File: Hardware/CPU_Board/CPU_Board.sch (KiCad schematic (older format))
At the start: 45 parts, among them P1 CONN_01X02, P2 USB_B, P3 CONN_01X06, P4 CONN_01X01, P5 CONN_01X01, P6 CONN_01X01, P7 CONN_01X01, P8 CONN_01X01, P9 CONN_01X01, U1 UA78M05IDCY, U2 UA78M33CDCY, U3 STM32F411RETx, U4 FT232RL, U5 TRACO_POWER_TEL_2-0511, Y1 8MHz

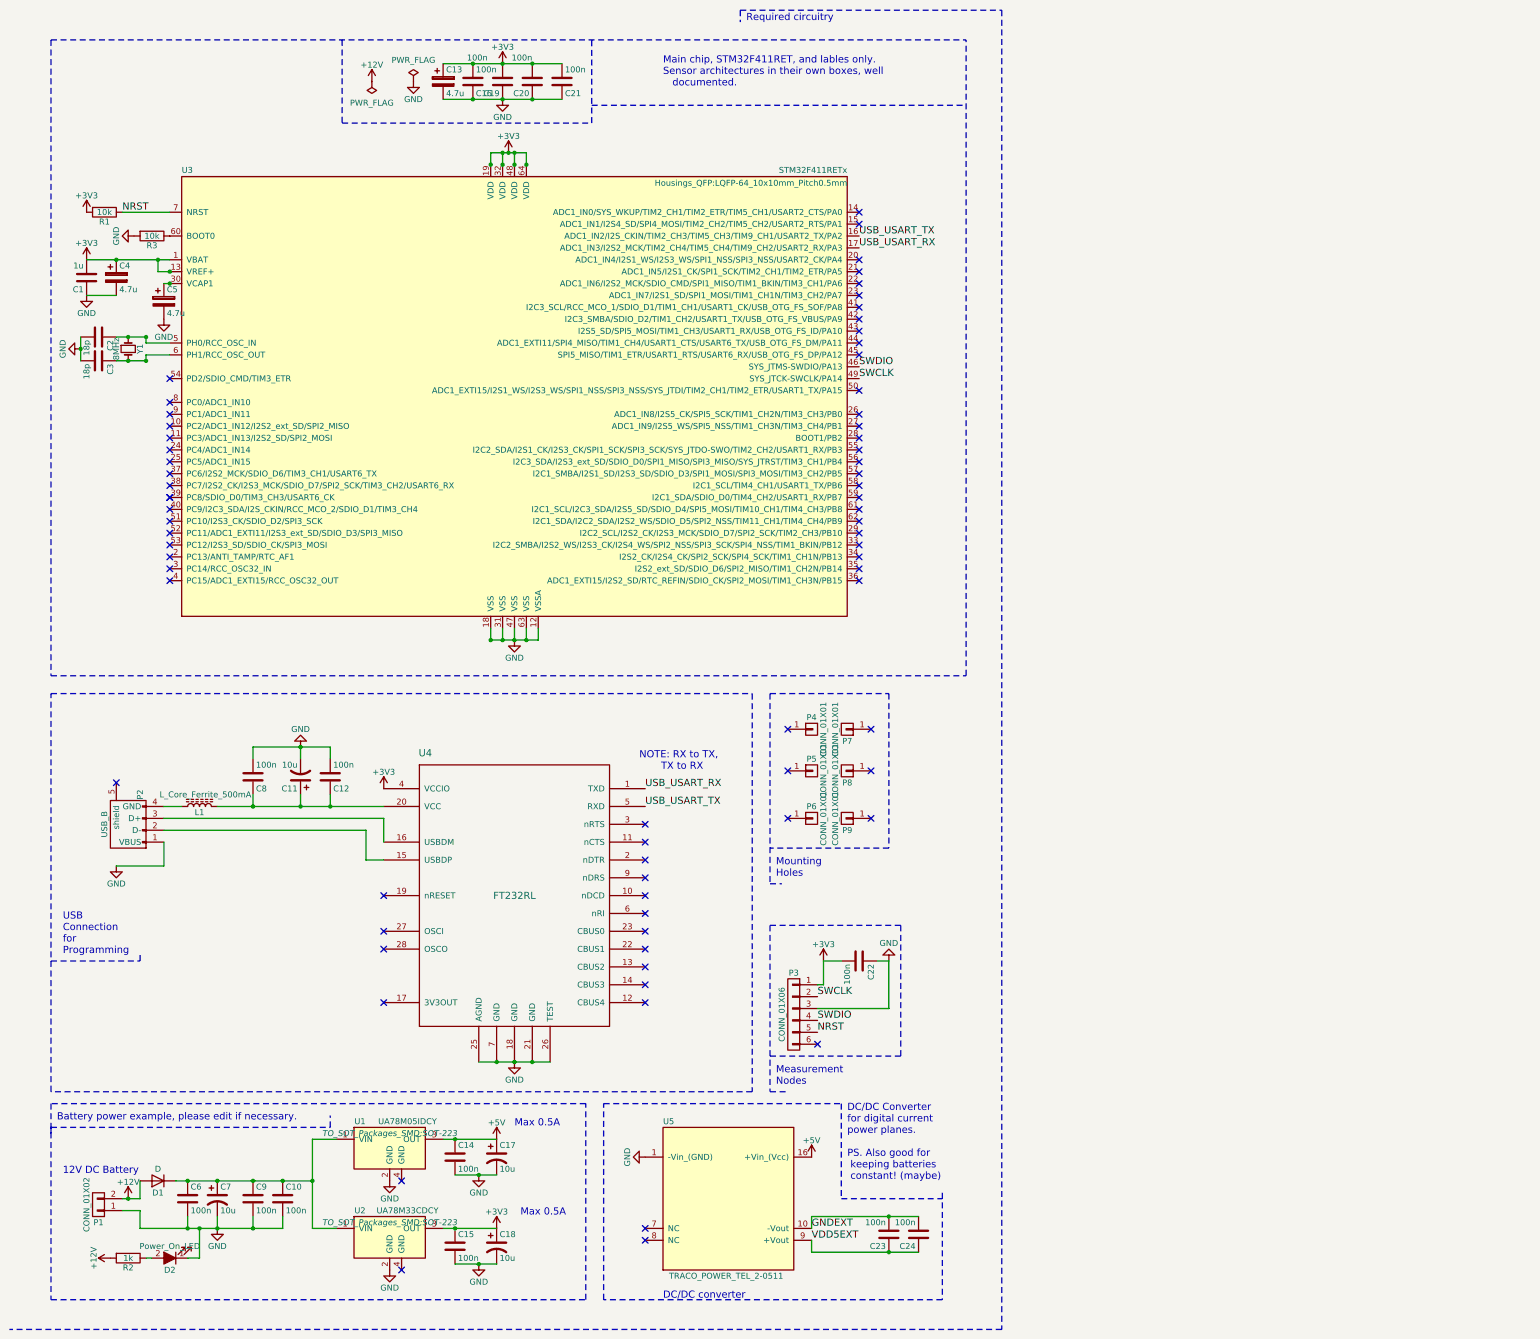
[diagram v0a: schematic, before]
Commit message: GPS, libraries and datasheet list
GPS: A2235-h added to schematic in UART settings. ON-OFF not finished!

Libraries:
- DCDCconv, ft232rl, lm1117, max3485e, stm32 (from kicad std-lib),
stm32f100, stm32f4.
* CUSTOM
- A2235-H

Datasheet:
- STM32 Ref. manual, Datasheet
- A2235-H Users manual
- Pa6H Datasheet
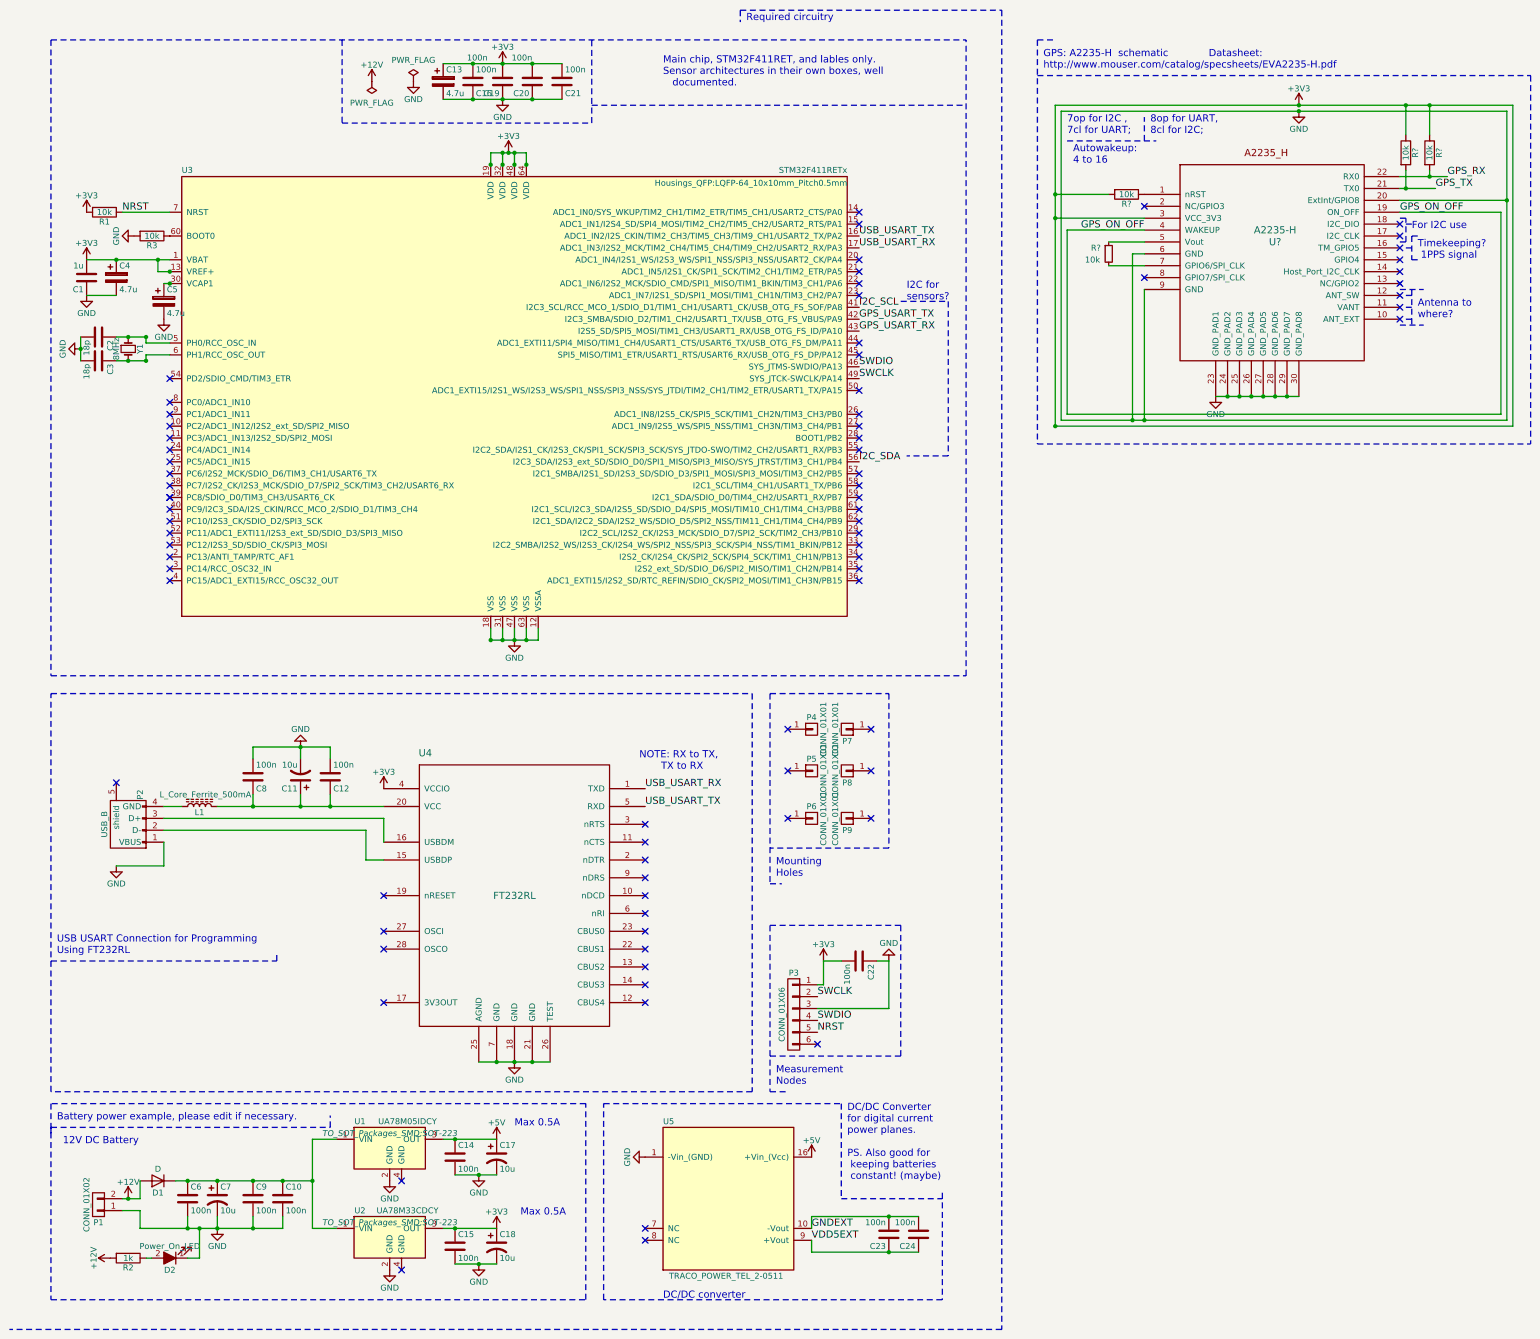
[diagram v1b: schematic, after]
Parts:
- added R?: 10k, symbol R_Small
- added R? (x3): 10k, symbol R
- added U?: A2235-H, symbol A2235-H
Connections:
- net +3V3: now also R?.1, R?.1, R?.2, U?.3 (VCC_3V3)
- net GND: now also U?.20 (ExtInt/GPIO8), U?.23 (GND_PAD1), U?.24 (GND_PAD2), U?.25 (GND_PAD3), U?.26 (GND_PAD4), U?.27 (GND_PAD5), U?.28 (GND_PAD6), U?.29 (GND_PAD7), U?.30 (GND_PAD8), U?.6 (GND), U?.9 (GND)
- net I2C_SCL: now reaches U3.41 (I2C3_SCL/RCC_MCO_1/SDIO_D1/TIM1_CH1/USART1_CK/USB_OTG_FS_SOF/PA8)
- net GPS_USART_TX: now reaches U3.42 (I2C3_SMBA/SDIO_D2/TIM1_CH2/USART1_TX/USB_OTG_FS_VBUS/PA9)
- net GPS_USART_RX: now reaches U3.43 (I2S5_SD/SPI5_MOSI/TIM1_CH3/USART1_RX/USB_OTG_FS_ID/PA10)
- net I2C_SDA: now reaches U3.56 (I2C3_SDA/I2S3_ext_SD/SDIO_D0/SPI1_MISO/SPI3_MISO/SYS_JTRST/TIM3_CH1/PB4)
- new net: R?.1, U?.1 (nRST)
- new net: R?.1, U?.5 (Vout)
- new net: R?.2, U?.7 (GPIO6/SPI_CLK)
- new net GPS_ON_OFF: U?.19 (ON_OFF), U?.4 (WAKEUP)
- new net GPS_RX: R?.2, U?.22 (RX0)
- new net GPS_TX: R?.2, U?.21 (TX0)
- no-connect marks 72 -> 79
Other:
- note added: "7op for I2C ,\n7cl for UART;"
- note added: "8op for UART,\n8cl for I2C;"
- note added: "Antenna to\nwhere?"
- note added: "Autowakeup:\n4 to 16"
- note added: "For I2C use"
- note added: "GPS: A2235-H schematic Datasheet:\nhttp://www.mouser.com/catalog/specsheets/EVA2235-H.pdf"
- note added: "I2C for\nsensors?"
- note added: "Timekeeping?\n 1PPS signal"
- note added: "USB USART Connection for Programming\nUsing FT232RL"
- note removed: "USB\nConnection\nfor\nProgramming"

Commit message: GPS proper shut-ON/OFF logic
Possible solution to support startup/shutdown sequence (GPIO - PA11).
Might take away filter and add a second logical gate for faster (more
true digital) switching.
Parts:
- added C? (x2): 100n, symbol C
- added C?: 100n, symbol C_Small
- added Q?: 2N7002 PLACEHOLDER, TO_SOT_Packages_SMD:SOT-23, symbol 2N7002
- added R?: 10k, symbol R
- added R?: 220, symbol R
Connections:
- net labels added: GPS_TOGGLE
- net labels removed: GPS_ON_OFF
- wire segments 158 -> 108
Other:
- note added: "Antenna?\nTo where?"
- note added: "Filter speed\n1ms"
- note added: "GPS"
- note added: "Pullups"
- note removed: "Antenna to\nwhere?"
- moved on the sheet: R?

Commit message: Libs and done first sketch GPS
Added depleted MOSFET library
Completed GPS wiring
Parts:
- removed C?: 100n, symbol C
- removed Q?: 2N7002 PLACEHOLDER, TO_SOT_Packages_SMD:SOT-23, symbol 2N7002
- removed R?: 10k, symbol R
- removed R?: 220, symbol R
- added Q?: P-Channel, symbol P-Channel
- added Q?: N-Channel, symbol N-Channel
- added R? (x3): 1k, symbol R
- added R?: 10k, symbol R
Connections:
- wire segments 108 -> 183
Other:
- note added: "3V3/2 =\n1.65V"
- note added: "High-speed digital \nswitching logic"
- note added: "Pull to\nReference"
- note removed: "Filter speed\n1ms"

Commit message: Shematic merger and stuff
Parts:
- added C?: 220nF, symbol C_Small
- added C? (x4): 100nF, symbol C_Small
- added C?: 10uF, symbol CP1_Small
- added C? (x5): 100n, Capacitors_SMD:C_0805_HandSoldering, symbol C
- added C? (x2): 10u, Capacitors_SMD:CP_Elec_5x5.8, symbol CP1
- added D?: D_Zener, symbol D_Zener
- added L? (x2): 330uH, symbol L
- added P?: CONN_01X04, symbol CONN_01X04
- added P?: CONN_01X02, Connect:AK300-2, symbol CONN_01X02
- added Q?: Q_PMOS_GSD, TO_SOT_Packages_SMD:SOT-23_Handsoldering, symbol Q_PMOS_GSD
- added Q? (x2): Q_PNP_BCE, TO_SOT_Packages_SMD:SOT-23_Handsoldering, symbol Q_PNP_BCE
- added R?: 5360, symbol R
- added R?: 2.7k, Resistors_SMD:R_0805_HandSoldering, symbol R
- added R? (x2): 6.8k, Resistors_SMD:R_0805_HandSoldering, symbol R
- added U?: INA128, symbol INA128
- added U?: LSM6DSL, symbol LSM6DSL
- added U?: LSM303AGR, symbol LSM303AGR
- added U?: LM1117ADJ, symbol LM1117ADJ
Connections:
- net +3V3: now also C?.1, C?.1, C?.1, C?.1, C?.1, C?.1, C?.1, L?.2, U?.1 (SA0), U?.10 (VDD_IO), U?.12 (CS), U?.2 (CS_XL), U?.2 (SDx), U?.2 (Vout), U?.3 (CS_MAG), U?.3 (SCx), U?.4 (Vout2), U?.5 (VDDIO), U?.8 (VDD), U?.9 (VDD)
- net +5V: now also P?.2 (P2), P?.4 (P4), Q?.3 (D), U?.7 (V+)
- net GND: now also C?.2, C?.2, C?.2, C?.2, C?.2, C?.2, C?.2, C?.2, C?.2, C?.2, C?.2, D?.2 (A), P?.1 (P1), P?.1 (P1), Q?.1 (G), R?.1, U?.1 (ADJ), U?.4 (V-), U?.5 (Ref), U?.6 (GND), U?.6 (GND), U?.7 (GND), U?.8 (GND)
- net Load_cell_amp: now reaches U3.8 (PC0/ADC1_IN10)
- net Load_cell_amp: now also U?.6
- net I2C_SCL renamed IMU_I2C_CL
- net IMU_I2C_CL: now also U?.1 (SCL), U?.13 (SCL)
- net I2C_SDA renamed IMU_I2C_DA
- net IMU_I2C_DA: now also U?.14 (SDA), U?.4 (SDA)
- new net: R?.1, U?.1 (Rg)
- new net: P?.2 (P2), U?.2 (-)
- new net: P?.3 (P3), U?.3 (+)
- new net: R?.2, U?.8 (Rg)
- new net: C?.1, U?.5 (C1)
- new net: C?.1, C?.1, C?.1, L?.2, Q?.2 (C), U?.3 (Vin)
- new net: Q?.2 (S), Q?.3 (E), Q?.3 (E), R?.1
- new net: D?.1 (K), R?.2, R?.2
- new net: Q?.1 (B), R?.1
- new net: Q?.1 (B), Q?.2 (C), R?.2
- new net +3.3VADC: C?.1, L?.1
- new net +5VA: C?.1, L?.1
- new net GNDA: C?.2, C?.2
- new net LSM303AGR_INT_1_XL: U?.11 (INT_2_XL), U?.12 (INT_1_XL)
- new net LSM303AGR_INT_MAG: U?.7 (INT_MAG/DRDY)
- new net LSM6DSL_INT1: U?.4 (INT1)
- new net LSM6DSL_INT2: U?.9 (INT2)
- no-connect marks 79 -> 78
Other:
- note added: "Amplifier for load cell,\nconnects to TH and Analog"
- note added: "I2C1 och I2C2 är ihopkopplade \nsom standard på IKS01A2. Vi får \nvälja vilken vi ska använda och \nså kan vi strunta i den andra."
- note added: "IMU"
- note added: "IMU circuitry"
- note added: "LSM303AGR VDD\nDecoup. Cap."
- note added: "LSM303AGR VDD_IO\nDecoup. Cap."
- note added: "LSM6DSL VDD\nDecoup. Cap."
- note added: "LSM6DSL VDD_IO\nDecoup. Cap."
- note added: "Outputs?"
- note removed: "I2C for\nsensors?"
- moved on the sheet: C?, Q?, R?, U?

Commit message: stuff
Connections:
- net LSM303AGR_INT_1_XL: no longer U?.11 (INT_2_XL)
- new net LSM303AGR_INT_2_XL: U?.11 (INT_2_XL)
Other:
- note added: "MCU Connects?"
- note removed: "Outputs?"
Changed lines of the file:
@@
 LIBS:a2235-h
 LIBS:MOSFET_depleted
+LIBS:misc_rfcom
 LIBS:CPU_Board-cache
-LIBS:IMU_Circuit-cache
-LIBS:PowerSupplySA-cache
 EELAYER 25 0
 EELAYER END
@@
 LSM303AGR_INT_1_XL
 Text Label 16100 2250 2    60   ~ 0
-LSM303AGR_INT_1_XL
+LSM303AGR_INT_2_XL
 Text Label 16100 4150 2    60   ~ 0
 LSM6DSL_INT1
@@
 IMU circuitry
 Text Notes 14950 3600 0    60   ~ 0
-Outputs?
+MCU Connects?
 Text Label 7650 3050 0    60   ~ 0
 IMU_I2C_CL

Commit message: Shitload of hardware stuff
* Added libraries
* Added footprints
* Moved stuff and updated local libraries (Hardware ->
schematic_modules)
* Drawn some footprints (LGA-14)
* Edited library (BT had two 5 pin)
* Added Octocouplers to protect BT (not yet implemented)
* Ran all CvPCB
* Divided all PCB components to fields, ready to be designed.
* Added shitload of datasheets to DOCS & Datasheets.txt
* Probably something else, but I'm sleepy
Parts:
- removed C10, C14, C15, C23, C24, C6, C9: 100n, Capacitors_SMD:C_0603_HandSoldering, symbol C
- removed C17, C18, C7: 10u, Capacitors_Tantalum_SMD:CP_Tantalum_Case-A_EIA-3216-18_Reflow, symbol CP1
- removed C?: 100n, symbol C
- removed D1: D, Diodes_SMD:D_SOD-123, symbol D
- removed D2: Power_On_LED, symbol LED_ALT
- removed P1: CONN_01X02, Pin_Headers:Pin_Header_Straight_2x01_Pitch2.54mm, symbol CONN_01X02
- removed R2: 1k, Resistors_SMD:R_0603_HandSoldering, symbol R
- removed U1: UA78M05IDCY, TO_SOT_Packages_SMD:SOT-223, symbol LT1129CST-5
- removed U2: UA78M33CDCY, TO_SOT_Packages_SMD:SOT-223, symbol LT1129CST-3.3
- removed U5: TRACO_POWER_TEL_2-0511, LIBRARIES:TRACO_POWER_TEX_2-0511, symbol TRACO_POWER_TEL_2-0511
- added C23: 1uF, Capacitors_ThroughHole:C_Axial_L3.8mm_D2.6mm_P7.50mm_Horizontal, symbol C_Small
- added R10: 47K, Resistors_ThroughHole:R_Axial_DIN0204_L3.6mm_D1.6mm_P5.08mm_Horizontal, symbol R_Small
- added R14: 0C, Resistors_ThroughHole:R_Axial_DIN0204_L3.6mm_D1.6mm_P1.90mm_Vertical, symbol R_Small
- added R6, R9: 10K, Resistors_ThroughHole:R_Axial_DIN0204_L3.6mm_D1.6mm_P5.08mm_Horizontal, symbol R_Small
- added U4: 6N136, Housings_DIP:DIP-8_W7.62mm_Socket, symbol 6N136
- added U5: SPBTLE-RF, RF_Modules:ST_SPBTLE, symbol SPBTLE-RF
- C1, C2, C3: footprint Capacitors_SMD:C_0603_HandSoldering -> Capacitors_ThroughHole:C_Axial_L3.8mm_D2.6mm_P7.50mm_Horizontal
- C10, C12, C18, C20, C9: renamed from C?; footprint Capacitors_SMD:C_0805_HandSoldering -> Capacitors_ThroughHole:C_Axial_L3.8mm_D2.6mm_P7.50mm_Horizontal
- C11: renamed from C13; footprint Capacitors_Tantalum_SMD:CP_Tantalum_Case-A_EIA-3216-18_Reflow -> Capacitors_ThroughHole:CP_Axial_L10.0mm_D4.5mm_P15.00mm_Horizontal
- C13, C19: renamed from C?; footprint Capacitors_SMD:CP_Elec_5x5.8 -> Capacitors_ThroughHole:CP_Axial_L10.0mm_D4.5mm_P15.00mm_Horizontal
- C14: renamed from C16; footprint Capacitors_SMD:C_0603_HandSoldering -> Capacitors_ThroughHole:C_Axial_L3.8mm_D2.6mm_P7.50mm_Horizontal
- C15: renamed from C19; footprint Capacitors_SMD:C_0603_HandSoldering -> Capacitors_ThroughHole:C_Axial_L3.8mm_D2.6mm_P7.50mm_Horizontal
- C16: renamed from C20; footprint Capacitors_SMD:C_0603_HandSoldering -> Capacitors_ThroughHole:C_Axial_L3.8mm_D2.6mm_P7.50mm_Horizontal
- C17: renamed from C21; footprint Capacitors_SMD:C_0603_HandSoldering -> Capacitors_ThroughHole:C_Axial_L3.8mm_D2.6mm_P7.50mm_Horizontal
- C21: renamed from C22; footprint Capacitors_SMD:C_0603_HandSoldering -> Capacitors_ThroughHole:C_Axial_L3.8mm_D2.6mm_P7.50mm_Horizontal
- C24, C25, C27, C28, C29, C30: renamed from C?; footprint (none) -> Capacitors_ThroughHole:C_Axial_L3.8mm_D2.6mm_P7.50mm_Horizontal
- C26: renamed from C?; footprint (none) -> Capacitors_ThroughHole:CP_Axial_L10.0mm_D4.5mm_P15.00mm_Horizontal
- C4, C5: footprint Capacitors_Tantalum_SMD:CP_Tantalum_Case-A_EIA-3216-18_Reflow -> Capacitors_ThroughHole:CP_Axial_L10.0mm_D4.5mm_P15.00mm_Horizontal
- C6: renamed from C8; footprint Capacitors_SMD:C_0603_HandSoldering -> Capacitors_ThroughHole:C_Axial_L3.8mm_D2.6mm_P7.50mm_Horizontal
- C7: renamed from C11; footprint Capacitors_Tantalum_SMD:CP_Tantalum_Case-A_EIA-3216-18_Reflow -> Capacitors_ThroughHole:CP_Axial_L10.0mm_D4.5mm_P15.00mm_Horizontal
- C8: renamed from C12; footprint Capacitors_SMD:C_0603_HandSoldering -> Capacitors_ThroughHole:C_Axial_L3.8mm_D2.6mm_P7.50mm_Horizontal
- D1: renamed from D?; footprint (none) -> Diodes_ThroughHole:D_5W_P5.08mm_Vertical_AnodeUp
- L1: footprint (none) -> Resistors_SMD:R_1206_HandSoldering
- L2, L3: renamed from L?; footprint (none) -> Connectors:bornier2
- P10: renamed from P?; footprint (none) -> Pin_Headers:Pin_Header_Straight_1x04_Pitch2.54mm
- P2: footprint (none) -> Connect:USB_B
- Q4, Q5: renamed from Q?; footprint (none) -> TO_SOT_Packages_SMD:SOT-23_Handsoldering
- R1: footprint Resistors_SMD:R_0603_HandSoldering -> Resistors_ThroughHole:R_Axial_DIN0204_L3.6mm_D1.6mm_P5.08mm_Horizontal
- R11, R12, R13, R15, R16, R17, R18, R7, R8: renamed from R?; footprint (none) -> Resistors_ThroughHole:R_Axial_DIN0204_L3.6mm_D1.6mm_P5.08mm_Horizontal
- R2: renamed from R3; footprint Resistors_SMD:R_0603_HandSoldering -> Resistors_ThroughHole:R_Axial_DIN0204_L3.6mm_D1.6mm_P5.08mm_Horizontal
- R3, R4, R5: renamed from R?; footprint Resistors_SMD:R_0805_HandSoldering -> Resistors_ThroughHole:R_Axial_DIN0204_L3.6mm_D1.6mm_P5.08mm_Horizontal
- U3: renamed from U?; footprint (none) -> TO_SOT_Packages_SMD:SOT-223
- U6: renamed from U?; footprint (none) -> FOOTPRINTS:A2235-H
- U7: renamed from U?; footprint (none) -> Housings_LGA:LGA-12_2x2mm_Pitch0.5mm
- U8: renamed from U?; footprint (none) -> FOOTPRINTS:LGA-14
- U9: renamed from U?; footprint (none) -> Housings_SOIC:SO-8_5.3x6.2mm_Pitch1.27mm
- gave numbers to parts that had none: 4
- renumbered U3 to U1, U4 to U2
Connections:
- net +3V3: now also C23.1, R6.2, R9.2, U5.5 (VIN)
- net +5V: no longer P10.4 (P4), U9.7 (V+)
- net +5VA: now also P10.4 (P4), U9.7 (V+)
- net GND: now also C23.2, R10.1, U5.6 (GND); no longer P10.1 (P1), U9.4 (V-), U9.5 (Ref)
- net GNDA: now also P10.1 (P1), U9.4 (V-), U9.5 (Ref)
- net GPS_TOGGLE: now also R14.2
- net at Q4.2 (S), Q5.2 (S), R15.2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: now also R14.1
- new net BT_10_PA1: R6.1, U5.10 (SPI_CS)
- new net BT_11_PA8: R9.1, U5.11 (~BT_RESET~)
- new net BT_5_PA0: R10.2, U5.4 (SPI_IRQ)
- new net BT_7_PB3: U5.7 (SPI_CLK)
- new net BT_8_PA6: U5.8 (SPI_MISO)
- new net BT_9_PA7: U5.9 (SPI_MOSI)
- no-connect marks 78 -> 83
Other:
- note added: "Bluetooth connection module"
- note added: "OctoAwesome"
- note added: "Power input from battery dock board"
- note removed: "12V DC Battery"
- note removed: "Battery power example, please edit if necessary."
- note removed: "DC/DC Converter\nfor digital current\npower planes.\n\nPS. Also good for\n keeping batteries \n constant! (maybe)"
- note removed: "DC/DC converter"
- note removed: "Max 0.5A"
- moved on the sheet: C10, C12, C13, C18, C19, C20, C25, C26, C27, C28, C29, C30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
